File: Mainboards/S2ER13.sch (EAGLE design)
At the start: 52 parts, among them IC1 LD1117S33, IC2 CC1101RTK, IC3 STM32F051C8, Q1 IRLML9301, Q2 8M, X1 VCC, X2 CLK, X3 GND, X4 DIO, X5 RST, X6 NC

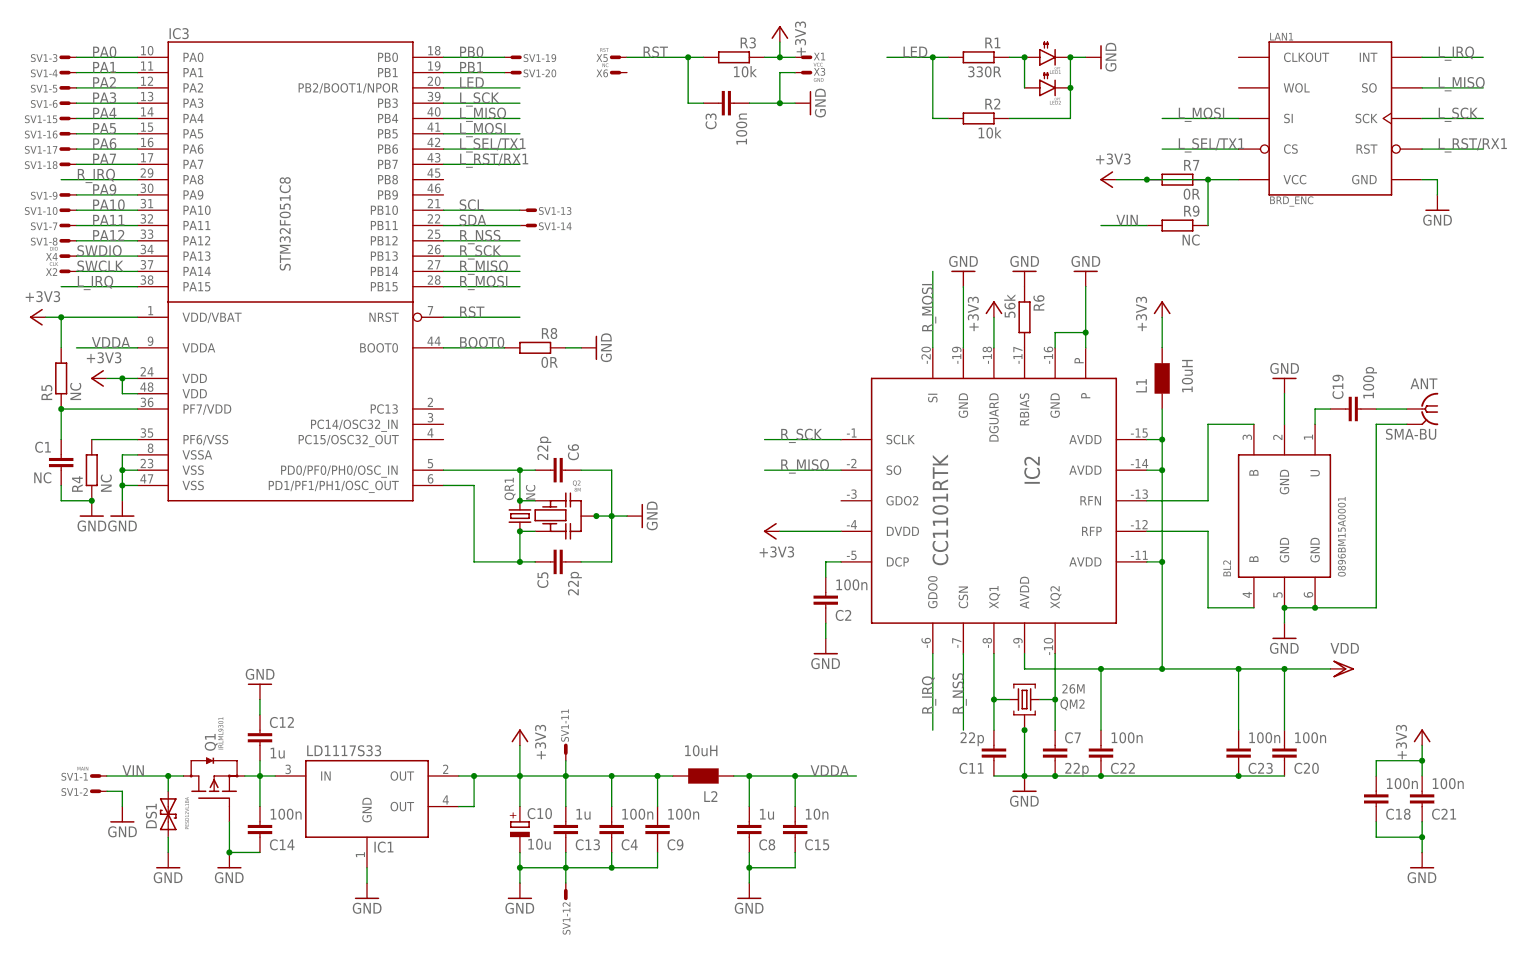
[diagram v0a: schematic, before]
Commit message: Added prototypes
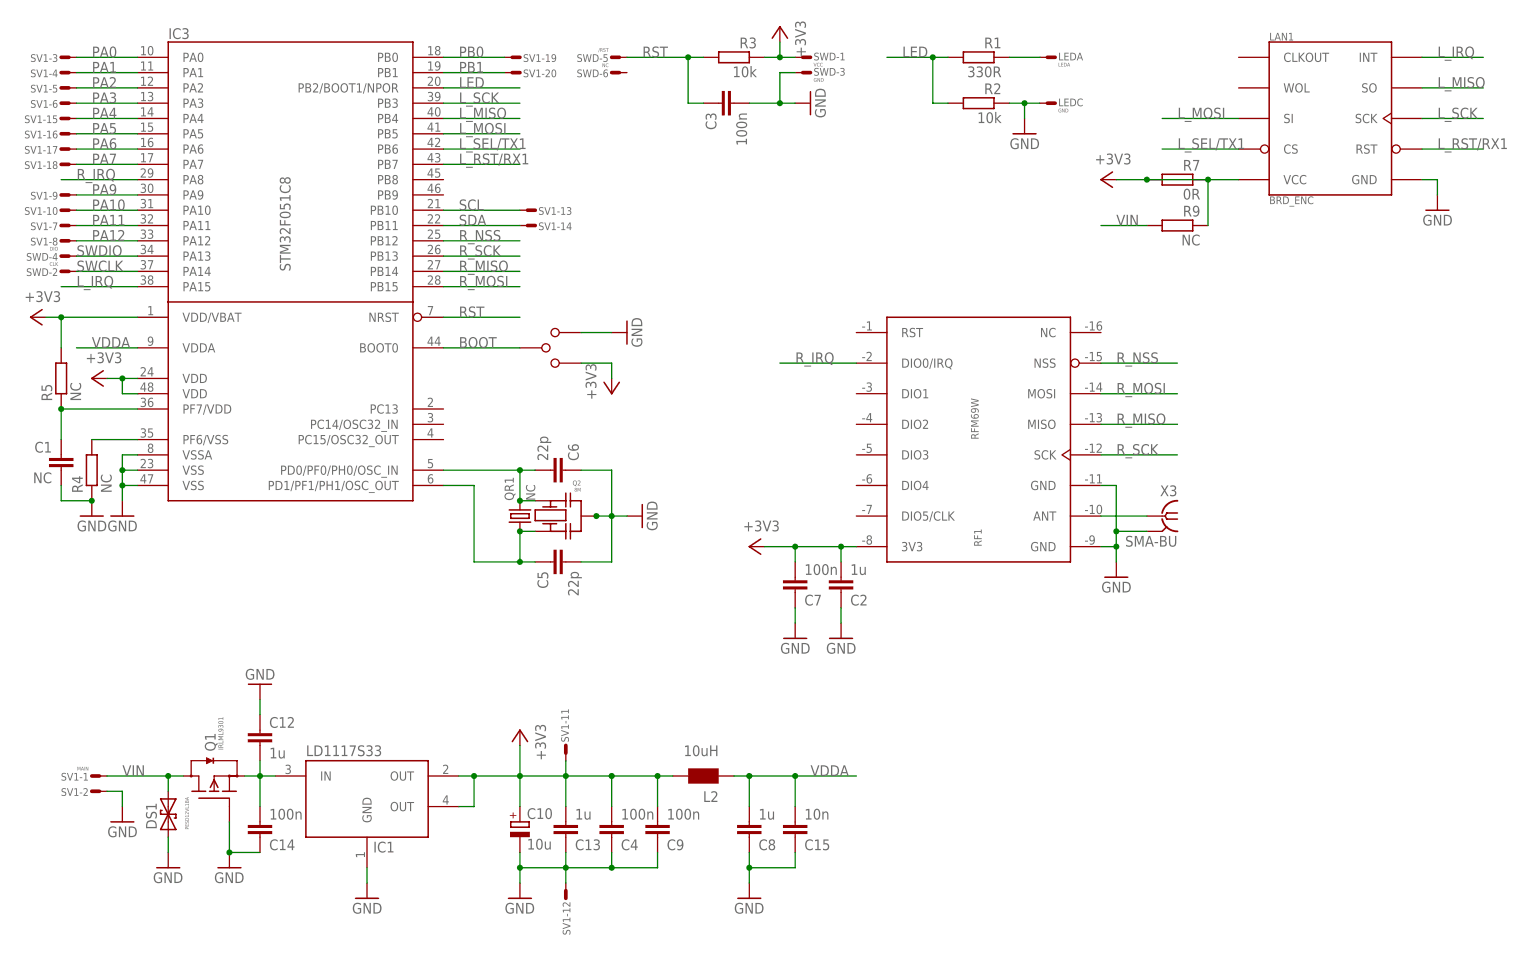
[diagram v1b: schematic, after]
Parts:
- removed ANT: SMA-BU, Conn:SMA-BU
- removed BL2: 0896BM15A0001, RF:BL
- removed C11: 22p, RCL:C0603
- removed C18, C20, C21, C22, C23: 100n, RCL:C0603
- removed C19: 100p, RCL:C0603
- removed IC2: CC1101RTK, RF:CC110LV
- removed L1: 10uH, RCL:L0603
- removed LED1: OPT, Optic:LEDT134
- removed LED2: OPT, Optic:LED1206
- removed QM2: 26M, QUARTZ:QM3.2X2.5
- removed R6: 56k, RCL:R0603
- removed R8: 0R, RCL:R0402
- added BR1: BR, Conn:BR
- added LEDA: LEDA, Conn:WIREPADT1.6/0.9
- added LEDC, SWD-3: GND, Conn:WIREPADT1.6/0.9
- added RF1: RFM69W, RF:RFM69
- C2: value 100n -> 1u
- C7: value 22p -> 100n
- SWD-5: value RST -> /RST
- X3: value GND -> SMA-BU; device Conn:WIREPADT1.6/0.9 -> Conn:SMA-BU
- renumbered X1 to SWD-1, X2 to SWD-2, X4 to SWD-4, X5 to SWD-5, X6 to SWD-6
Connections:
- removed net BOOT0: IC3.BOOT0, R8.2
- removed net N$11: C11.2, IC2.XQ1, QM2.2
- removed net N$12: C7.1, IC2.XQ2, QM2.1
- removed net N$13: BL2.U@1, C19.1
- removed net N$14: ANT.1, C19.2
- removed net N$6: IC2.RBIAS, R6.2
- removed net N$7: C2.2, IC2.DCP
- removed net N$8: BL2.B@3, IC2.RFN
- removed net N$9: BL2.B@4, IC2.RFP
- removed net VDD: C20.2, C22.2, C23.2, IC2.AVDD, IC2.AVDD@1, IC2.AVDD@2, IC2.AVDD@3, L1.1
- new net BOOT: BR1.M, IC3.BOOT0
- new net N$5: RF1.ANT, X3.1
- net +3V3: now also BR1.R, C2.2, C7.2, RF1.3V3; no longer C18.2, C21.2, IC2.DGUARD, IC2.DVDD, L1.2
- net GND: now also BR1.L, C7.1, LEDC.S, RF1.GND@11, RF1.GND@9, SWD-3.S, X3.2; no longer ANT.2, BL2.GND@2, BL2.GND@5, BL2.GND@6, C11.1, C18.1, C20.1, C21.1, C22.1, C23.1, C7.2, IC2.GND, IC2.GND@1, IC2.P, LED1.C, LED2.C, QM2.M1, QM2.M2, R6.1, R8.1, X3.S
- net N$1: now also LEDA.S; no longer LED1.A, LED2.A
- net R_IRQ: now also RF1.DIO0/IRQ; no longer IC2.GDO0
- net R_MISO: now also RF1.MISO; no longer IC2.SO
- net R_MOSI: now also RF1.MOSI; no longer IC2.SI
- net R_NSS: now also RF1.NSS; no longer IC2.CSN
- net R_SCK: now also RF1.SCK; no longer IC2.SCLK
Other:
- moved on the sheet: C2, C7, R2

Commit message: S2ER13 Proto
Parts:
- removed BR1: BR, Conn:BR
- removed LEDA: LEDA, Conn:WIREPADT1.6/0.9
- removed LEDC, SWD-3: GND, Conn:WIREPADT1.6/0.9
- added ANT: SMA-BU, Conn:SMA-BU
- added L1: 10uH, RCL:L0603
- added LED1: OPT, Optic:LEDT134
- added LED2: OPT, Optic:LED1206
- added R8: 10k, RCL:R0603
- added X7: BOOT0, Conn:WIREPADT1.6/0.9
- C2: value 1u -> 100n
- C7: value 100n -> 1u
- R4, R5: device RCL:R0402 -> RCL:R0603
- RF1: value RFM69W -> RFM69CW; device RF:RFM69 -> RF:RFM69CW-868-S1
- X3: value SMA-BU -> GND; device Conn:SMA-BU -> Conn:WIREPADT1.6/0.9
- X5: value /RST -> RST
- renumbered SWD-1 to X1, SWD-2 to X2, SWD-4 to X4, SWD-5 to X5, SWD-6 to X6
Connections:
- removed net BOOT: BR1.M, IC3.BOOT0
- new net BOOT0: IC3.BOOT0, R8.2, X7.S
- new net VDDR: C2.2, C7.1, L1.1, RF1.VDD
- net +3V3: now also L1.2; no longer BR1.R, C2.2, C7.2, RF1.3V3
- net GND: now also ANT.2, C7.2, LED1.C, LED2.C, R8.1, RF1.GND, RF1.GND@1, X3.S; no longer BR1.L, C7.1, LEDC.S, RF1.GND@11, RF1.GND@9, SWD-3.S, X3.2
- net N$1: now also LED1.A, LED2.A; no longer LEDA.S
- net N$5: now also ANT.1, RF1.ANA; no longer RF1.ANT, X3.1
- net R_IRQ: now also RF1.DIO0; no longer RF1.DIO0/IRQ
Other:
- moved on the sheet: C2, C7, R2
